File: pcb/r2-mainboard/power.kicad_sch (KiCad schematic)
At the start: 0 parts

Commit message: R2: capture power.kicad_sch -- the gated rail tree from +VSYS
WP2. Five converters, every one of them switchable, which is the whole
reason R2 exists: R1 wires four bucks' ~SHDN to +5V and 82% of idle
power sits on rails no firmware can reach.

  +3V3_AON   TPS7A0233   LDO, always on, 25 nA
  +5V_DCDC   TPS61022    boost, behind a TPS22965 load switch
  +3V3_DCDC  TPS63802    buck-boost
  +1V2_DCDC  TPS62A02    buck
  +1V35_DCDC TPS62A02    buck

Two findings changed the plan and are recorded in NOTES-R2-plan.md:

- A 1S cell cannot buck to 3.3 V. +VSYS runs 4.4 V down to 3.0 V, so a
  step-down converter drops out halfway down the discharge curve. +3V3
  is a buck-boost, and the two 3.3 V rails the plan called for become
  one, since each would cost a whole converter.
- A boost has no load disconnect. Disabling TPS61022 alone would leave
  ~3.4 V on the SoM's VIN pin, which is a partial-power state rather
  than off, so the disconnect goes on the boost's input instead.

Every EN carries a pull-down; the rails come up only when firmware asks.
PG pull-ups are 470k, not 10k, because a power-good pin is low whenever
its rail is off -- at 10k that is 3.3 mW of the 10 mW standby budget.
Converter overhead in standby works out to ~24 uA.

Verified with kicad-cli erc plus a node-by-node read of the exported
netlist. 25 violations, one of them real: battery.kicad_sch's +3V3_AON
PWR_FLAG is now redundant against U10's power_out pin. Left in place --
that sheet is out for review and editing it under an open Eeschema
session would discard unsaved work. docs/power.md §9 has the one-symbol
fix.

Nothing here has been built or measured.

Co-Authored-By: Claude Opus 5 <noreply@anthropic.com>
Claude-Session: https://claude.ai/code/session_01LsKada4AAxqV6Vzap4hwJf
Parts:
- added C20, C21: 1uF/16V, Capacitor_SMD:C_0402_1005Metric, symbol Device:C
- added C22, C25, C26, C27, C30: 22uF/10V, Capacitor_SMD:C_0805_2012Metric, symbol Device:C
- added C23: 470pF/50V, Capacitor_SMD:C_0402_1005Metric, symbol Device:C
- added C24: 100nF/16V, Capacitor_SMD:C_0402_1005Metric, symbol Device:C
- added C28: 100pF/50V, Capacitor_SMD:C_0402_1005Metric, symbol Device:C
- added C29: 10uF/10V, Capacitor_SMD:C_0805_2012Metric, symbol Device:C
- added C31, C33: 4.7uF/10V, Capacitor_SMD:C_0805_2012Metric, symbol Device:C
- added C32, C34: 22uF/6.3V, Capacitor_SMD:C_0805_2012Metric, symbol Device:C
- added L10, L12, L13: 1uH/6A, Inductor_SMD:L_1210_3225Metric, symbol Device:L
- added L11: 0.47uH/6A, Inductor_SMD:L_1008_2520Metric, symbol Device:L
- added R20, R26, R31, R35: 100k, Resistor_SMD:R_0402_1005Metric, symbol Device:R
- added R21: 732k/1%, Resistor_SMD:R_0402_1005Metric, symbol Device:R
- added R22, R29, R30, R34: 100k/1%, Resistor_SMD:R_0402_1005Metric, symbol Device:R
- added R23, R27: 0R, Resistor_SMD:R_0402_1005Metric, symbol Device:R
- added R24: 511k/1%, Resistor_SMD:R_0402_1005Metric, symbol Device:R
- added R25: 91k/1%, Resistor_SMD:R_0402_1005Metric, symbol Device:R
- added R28, R32, R36: 470k, Resistor_SMD:R_0402_1005Metric, symbol Device:R
- added R33: 124k/1%, Resistor_SMD:R_0402_1005Metric, symbol Device:R
- added U10: TPS7A0233DBVR, Package_TO_SOT_SMD:SOT-23-5, symbol r2:TPS7A0233DBV
- added U11: TPS22965DSGR, Package_SON:Texas_DSG0008A_WSON-8-1EP_2x2mm_P0.5mm_EP0.9x1.6mm, symbol r2:TPS22965DSG
- added U12: TPS61022RWUR, Package_DFN_QFN:Texas_RWU0007A_VQFN-7_2x2mm_P0.5mm, symbol Converter_DCDC:TPS61022
- added U13: TPS63802DLAR, r2:Texas_DLA0010A_VSON-HR-10_2x3mm_P0.5mm, symbol r2:TPS63802DLA
- added U14, U15: TPS62A02DRLR, Package_TO_SOT_SMD:SOT-563, symbol r2:TPS62A02DRL
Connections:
- new net: R33.2, R34.1, U15.5 (FB)
- new net: R27.1, U13.2 (MODE)
- new net: R24.2, R25.1, U13.4 (FB)
- new net: L11.2, U13.7 (L2)
- new net: L11.1, U13.9 (L1)
- new net: R29.2, R30.1, U14.5 (FB)
- new net: L13.1, U15.2 (SW)
- new net: L10.2, U12.2 (SW)
- new net: C28.2, R21.2, R22.1, U12.4 (FB)
- new net: L12.1, U14.2 (SW)
- new net: C23.1, U11.6 (CT)
- new net: R23.1, U12.6 (MODE)
- new net +1V2_DCDC: C32.1, L12.2, R29.1
- new net +1V35_DCDC: C34.1, L13.2, R33.1
- new net +3V3_AON: C21.1, R28.1, R32.1, R36.1, U10.5 (OUT)
- new net +3V3_DCDC: C30.1, R24.1, U13.6 (VOUT)
- new net +5V_DCDC: C26.1, C27.1, C28.1, R21.1, U12.3 (VOUT)
- new net +VSYS: C20.1, C22.1, C24.1, C29.1, C31.1, C33.1, U10.1 (IN), U10.3 (EN), U11.1 (VIN), U11.2 (VIN), U11.4 (VBIAS), U13.10 (VIN), U14.3 (VIN), U15.3 (VIN)
- new net GND: C20.2, C21.2, C22.2, C23.2, C24.2, C25.2, C26.2, C27.2, C29.2, C30.2, C31.2, C32.2, C33.2, C34.2, R20.2, R22.2, R23.2, R25.2, R26.2, R27.2, R30.2, R31.2, R34.2, R35.2, U10.2 (GND), U11.5 (GND), U11.9 (EP), U12.1 (GND), U13.3 (AGND), U13.8 (GND), U14.1 (GND), U15.1 (GND)
- new net MCU_EN_3V3: R26.1, U13.1 (EN)
- new net MCU_EN_5V: R20.1, U11.3 (ON)
- new net MCU_EN_DDR: R35.1, U15.4 (EN)
- new net MCU_EN_FPGA_CORE: R31.1, U14.4 (EN)
- new net PG_1V2: R32.2, U14.6 (PG)
- new net PG_1V35: R36.2, U15.6 (PG)
- new net PG_3V3: R28.2, U13.5 (PG)
- new net VSYS_SW: C25.1, L10.1, U11.7 (VOUT), U11.8 (VOUT), U12.5 (EN), U12.7 (VIN)
- no-connect marks 0 -> 1
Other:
- note added: "+1V2_DCDC — Spartan-6 VCCINT"
- note added: "+1V35_DCDC — DDR3L and the FPGA's DDR bank VCCO"
- note added: "+3V3_AON — always-on housekeeping rail"
- note added: "+3V3_DCDC — FPGA I/O, config NOR, microSD"
- note added: "+5V_DCDC — SoM VIN and the EPD HV chain"
- note added: "Buck-boost, not buck: a 1S cell cannot step down to 3.3 V."
- note added: "Dropout is 270 mV max at 200 mA, so the rail follows +VSYS down"
- note added: "ERC power flags"
- note added: "Every EN on this sheet is pulled down, so each rail is off until firmware asks for it."
- note added: "Only the two buck rails need one: their output is the far side"
- note added: "STM32G0, I2C pull-ups, buttons. 25 nA quiescent."
- note added: "That is the whole difference from R1, where four bucks had ~SHDN wired to +5V."
- note added: "True shutdown with load disconnect, so the rail is genuinely"
- note added: "U11 is the real disconnect; U12's EN follows its own switched input,"
- note added: "at low battery. Everything on it works below 3.3 V."
- note added: "of an inductor, so no pin declares itself a driver."
- note added: "off in standby."
- note added: "so one GPIO owns the pair and 'off' is unambiguous."
- note added: "to mcu.kicad_sch"

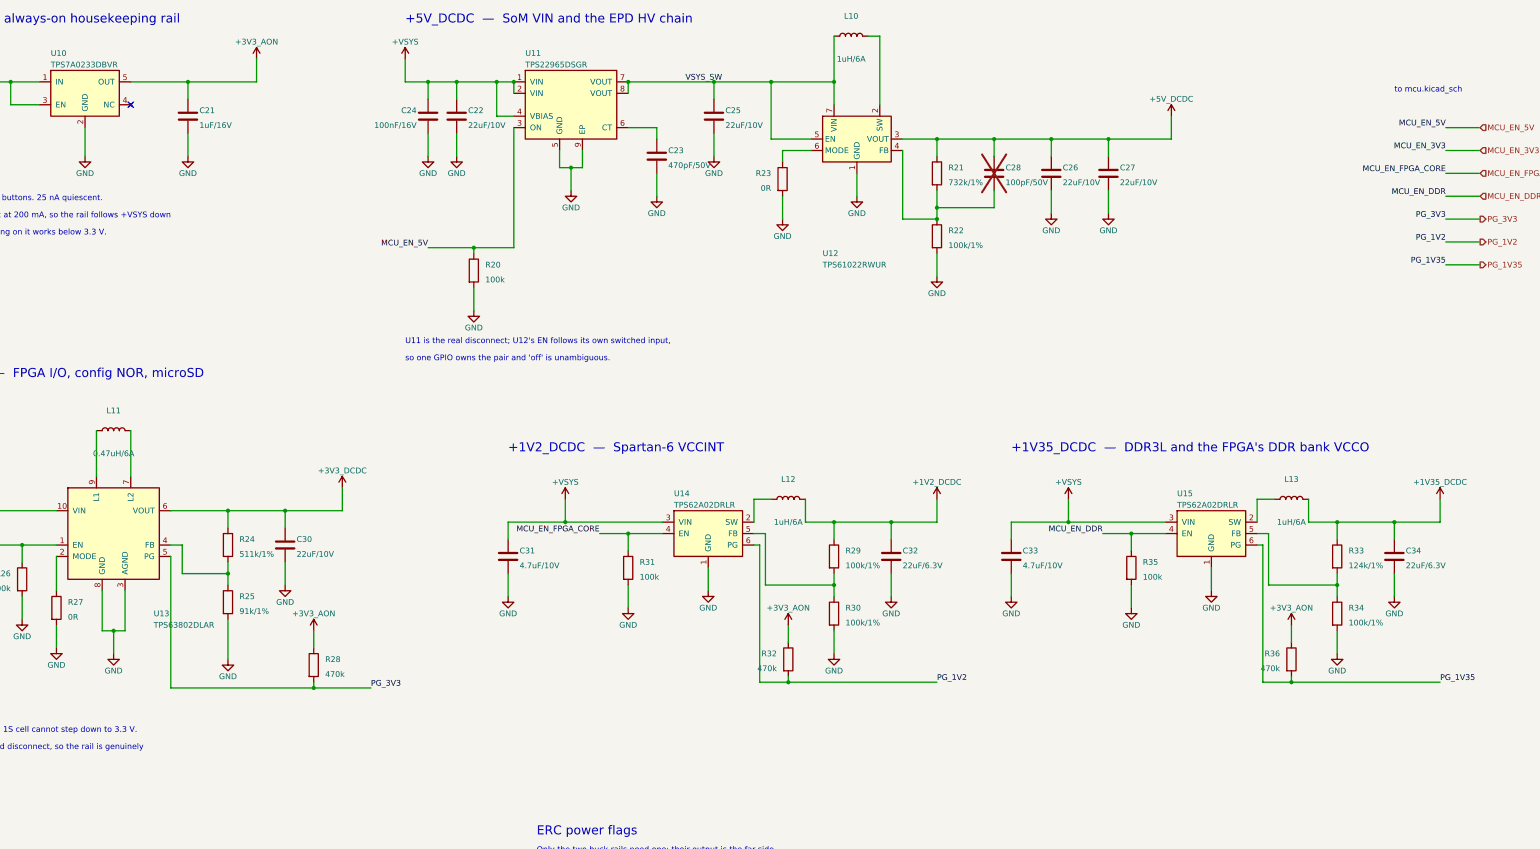
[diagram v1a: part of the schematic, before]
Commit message: R2: power sheet review pass 1 -- the TPS22965 load switch is deleted
power.kicad_sch was reviewed against manual-analysis/Analysis_power.md and
patched in place by tools/patch_power_review1.py. Once Eeschema has saved a
sheet it is the source of truth, so gen_power.py was not re-run.

The substantive finding: the TPS61022 boost already has true input/output
disconnect in shutdown -- datasheet Features (p.1), §7.3.2, and IVOUT_LKG in
§6.5, which is measured with VOUT forced to 5.5 V while VIN sits at 0 V.
docs/power.md §2.2 had misread §7.3.5, which describes pass-through while the
part is *enabled*. U11 (TPS22965) and its C23/C24 are therefore deleted, and
MCU_EN_5V drives U12.EN directly with R20 as the 100 k pull-down. That also
removes ~85 mW of RON loss at 2.3 A and ~30-50 uA of VBIAS quiescent.

Two value errors found while in there: all four inductors claimed 6 A where the
fitted DFE322512F-1R0M is Isat 4.8 A / Irms 3.8 A, and C32/C34 were 6.3 V where
tps62a01.pdf Table 8-3 specifies 10 V.

docs/power.md gains §10 -- all 13 review points answered from the datasheets
with the page or table cited, each closed as either changed or correct-as-drawn
-- and §11, the layout guidelines that §9 owed. §1-§9 and §13 are brought in
line with the patched sheet.

NOTES-R2-plan.md marks WP2 reviewed, withdraws the standing +5V_SOM load-switch
requirement, and closes standing asks 1 and 2 (the +3V3_AON PWR_FLAG must now
stay: after the +3V3_AON_DCDC rename it is the net's only ERC driver).

Verified: kicad-cli sch erc --format json reports 0 violations on /power/; the
netlist was node-diffed against the pre-patch sheet and shows only the intended
changes with no new unconnected-* nets; page 3 was rendered and inspected.

Also included: the owner's own review edits to battery.kicad_sch, and the review
notes moved from Analyse_battery.md to manual-analysis/.

Co-Authored-By: Claude Opus 5 <noreply@anthropic.com>
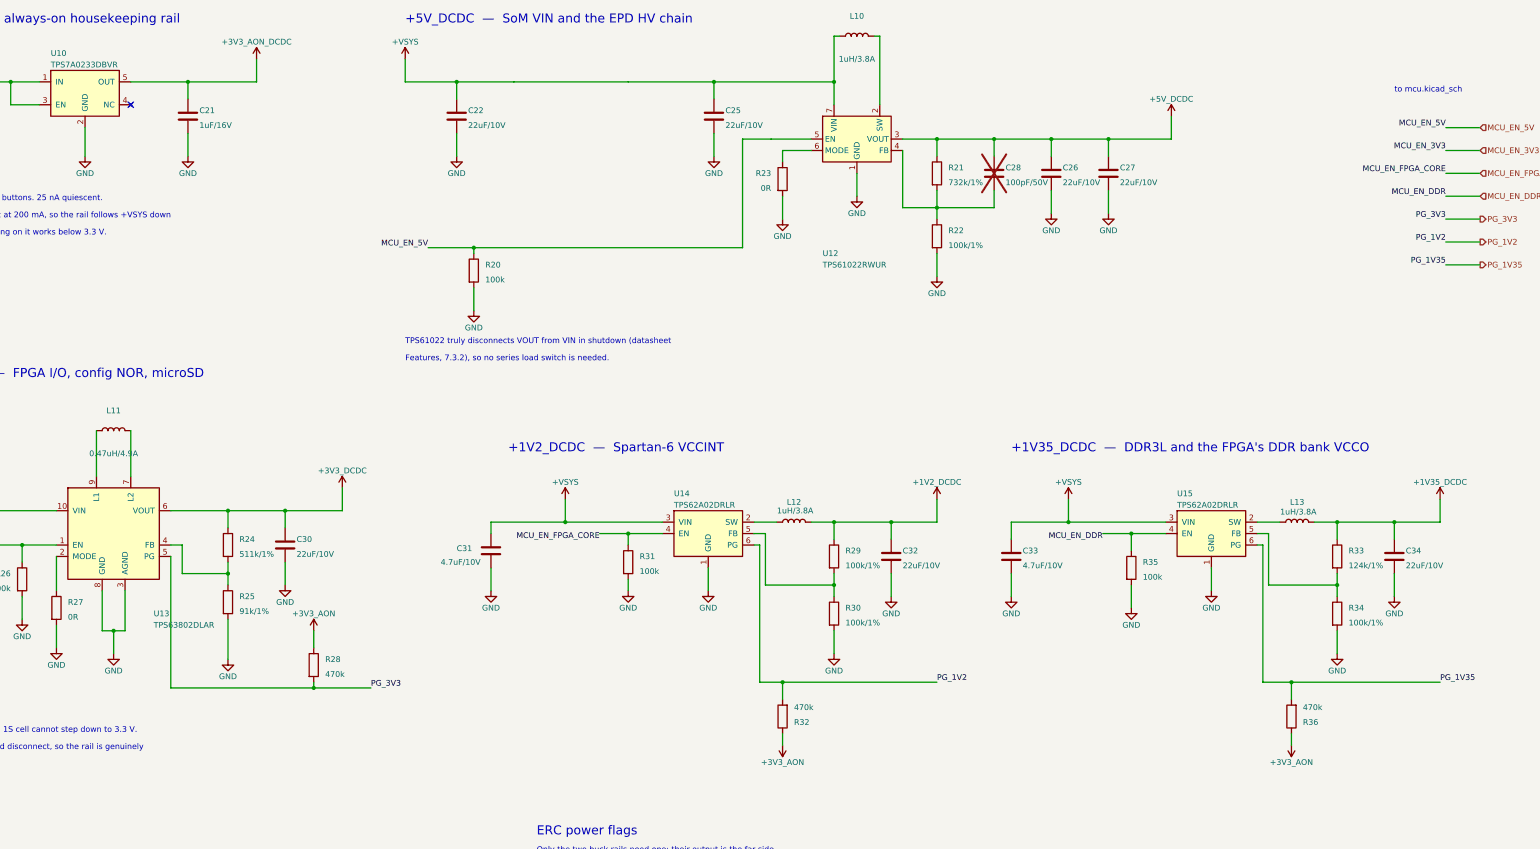
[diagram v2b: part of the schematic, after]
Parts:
- removed C23: 470pF/50V, Capacitor_SMD:C_0402_1005Metric, symbol Device:C
- removed C24: 100nF/16V, Capacitor_SMD:C_0402_1005Metric, symbol Device:C
- removed U11: TPS22965DSGR, Package_SON:Texas_DSG0008A_WSON-8-1EP_2x2mm_P0.5mm_EP0.9x1.6mm, symbol r2:TPS22965DSG
- C32, C34: value 22uF/6.3V -> 22uF/10V
- L10, L12, L13: value 1uH/6A -> 1uH/3.8A
- L11: value 0.47uH/6A -> 0.47uH/4.9A
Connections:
- net +3V3_AON: no longer C21.1, U10.5 (OUT)
- net +VSYS: now also C25.1, L10.1, U12.7 (VIN)
- net MCU_EN_5V: now also U12.5 (EN)
- removed net VSYS_SW: C25.1, L10.1, U12.5 (EN), U12.7 (VIN)
- new net +3V3_AON_DCDC: C21.1, U10.5 (OUT)
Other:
- note added: "Features, 7.3.2), so no series load switch is needed."
- note added: "TPS61022 truly disconnects VOUT from VIN in shutdown (datasheet"
- note removed: "U11 is the real disconnect; U12's EN follows its own switched input,"
- note removed: "so one GPIO owns the pair and 'off' is unambiguous."
- moved on the sheet: C31, L10, L12, L13, R31, R32, R36

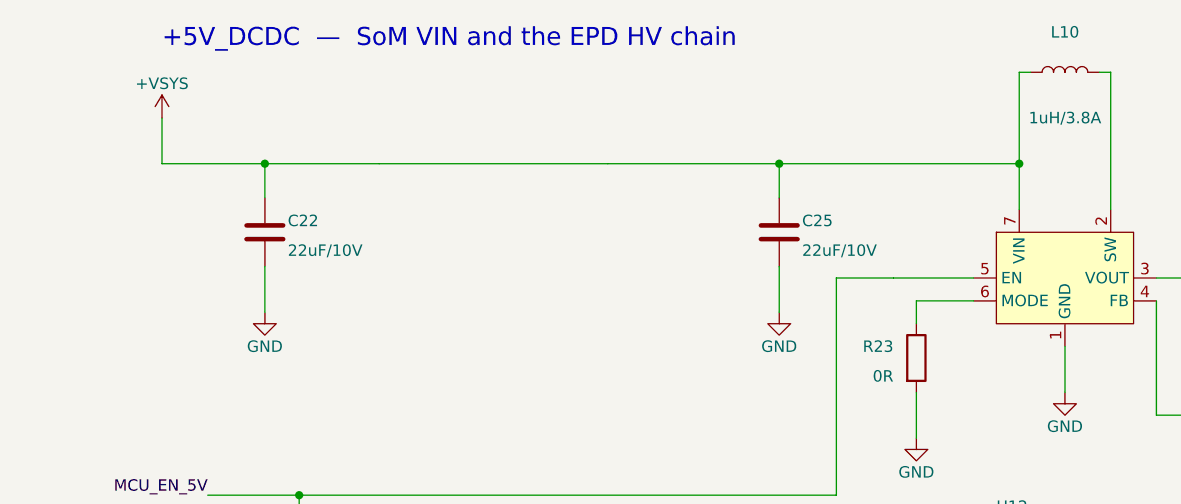
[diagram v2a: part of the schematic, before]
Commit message: R2: mcu sheet review pass 1, plus an R1 comparison
mcu.kicad_sch was reviewed against manual-analysis/Analysis_mcu.md and patched in
place by tools/patch_mcu_review1.py; gen_mcu.py was not re-run.

C42 is deleted. stm32g0b1.pdf Figure 15 (p.65) is the whole of ST's decoupling
scheme and it shows no capacitor on VBAT. With no coin cell fitted, pin 6 (VBAT)
is strapped to the same +3V3_AON net as pin 8 (VDD/VDDA) two pitches away, and
that net already carries C40 4.7 uF + C41 100 nF -- the figure's specified pair.
C42 was a third capacitor on an already-decoupled net.

SW21/SW22, the page buttons, move from TS-1187A-B-A-B to Panasonic EVQPLHA15:
same 1.6 N force and 1.5 mm travel, so the feel is unchanged, but 500 k cycles
instead of 100 k. At a plausible ~200 page turns a day the old part is rated for
about 1.4 years, and these are the most-actuated components on the board. SW20
stays a TS-1187A -- it is the power button, pressed rarely, and JLC Basic.

FB20 stays, but the doc now says plainly that no datasheet asks for it: Figure 15
feeds VREF+ with 100 nF + 1 uF and no series element. It is inherited from R1's
FB3, which was justified because the H750 brings VDDA out as its own pin; the G0
merges VDDA into VDD, so VREF+ is the only node left to filter. What makes it
safe is DCR rather than impedance -- Table 21 caps VREF+ at min(VDD + 0.4, 4.0) V
and BLM15AG121SN1D is 190 mOhm, so 0.19 mV at 1 mA. A resistor there would be a
hazard, and that constraint is now recorded on the part itself.

The 8 MHz the review found is the HSE, not Y20: Table 42 lists fOSC_IN as 4/8/48
MHz min/typ/max and Figure 20 is captioned "Typical application with an 8 MHz
crystal". Y20 is the LSE -- Table 43, on PC14/PC15. No HSE is fitted, which is
what frees PF0/PF1 for MCU_EN_5V/MCU_EN_3V3.

Datasheet 3.5 (p.16) lists the boot loader's interfaces and two are already on
this sheet: USART on PA9/PA10 (= MCU_TXD/MCU_RXD, with the SoM at the far end)
and USB on PA11/PA12 (two of the eleven spa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
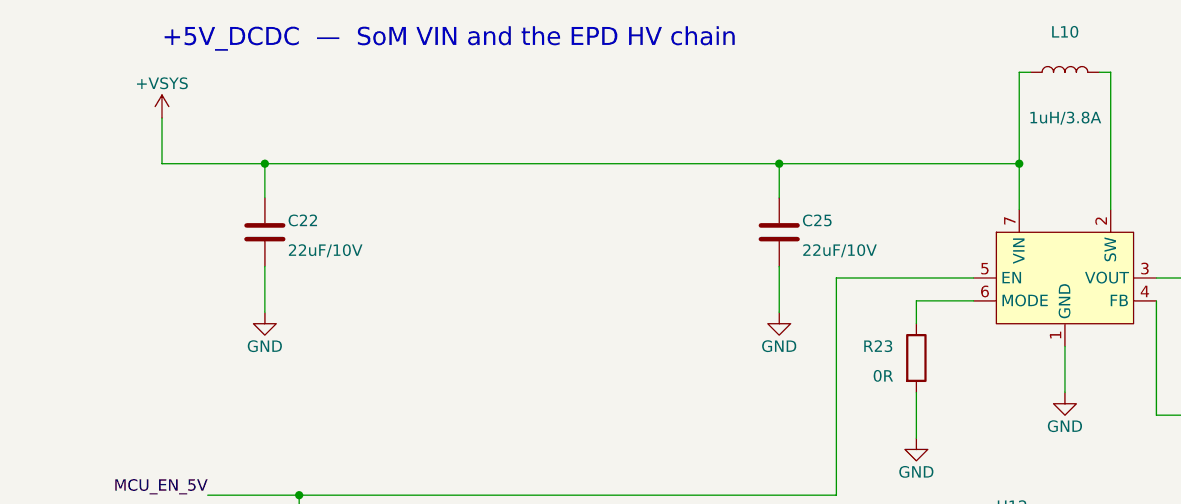
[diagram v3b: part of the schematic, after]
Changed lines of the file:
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@@
 	(wire
 		(pts
-			(xy 140.97 58.42) (xy 165.1 58.42)
+			(xy 140.97 58.42) (xy 236.22 58.42)
 		)
 		(stroke
@@
 	(wire
 		(pts
+			(xy 146.05 95.25) (xy 215.9 95.25)
+		)
+		(stroke
+			(width 0)
+			(type default)
+		)
+	)
+	(wire
+		(pts
 			(xy 370.84 156.21) (xy 370.84 151.13)
 		)
@@
 	(wire
 		(pts
-			(xy 222.25 71.12) (xy 231.14 71.12)
-		)
-		(stroke
-			(width 0)
-			(type default)
-		)
-	)
-	(wire
-		(pts
 			(xy 236.22 180.34) (xy 236.22 185.42)
 		)
@@
 	(wire
 		(pts
-			(xy 245.11 48.26) (xy 246.38 48.26)
+			(xy 215.9 95.25) (xy 215.9 71.12)
 		)
 		(stroke
@@
 	(wire
 		(pts
-			(xy 231.14 73.66) (xy 224.79 73.66)
+			(xy 245.11 48.26) (xy 246.38 48.26)
 		)
 		(stroke
@@
 	(wire
 		(pts
-			(xy 297.18 71.12) (xy 297.18 74.93)
+			(xy 231.14 73.66) (xy 224.79 73.66)
 		)
 		(stroke
@@
 	(wire
 		(pts
-			(xy 190.5 58.42) (xy 236.22 58.42)
+			(xy 297.18 71.12) (xy 297.18 74.93)
 		)
 		(stroke
@@
 	(wire
 		(pts
+			(xy 215.9 71.12) (xy 231.14 71.12)
+		)
+		(stroke
+			(width 0)
+			(type default)
+		)
+	)
+	(wire
+		(pts
 			(xy 88.9 153.67) (xy 127 153.67)
 		)
@@
 		)
 	)
-	(wire
-		(pts
-			(xy 165.1 58.42) (xy 190.5 58.42)
-		)
-		(stroke
-			(width 0)
-			(type default)
-		)
-	)
-	(wire
-		(pts
-			(xy 146.05 95.25) (xy 215.9 95.25)
-		)
-		(stroke
-			(width 0)
-			(type default)
-		)
-	)
-	(wire
-		(pts
-			(xy 215.9 95.25) (xy 215.9 71.12)
-		)
-		(stroke
-			(width 0)
-			(type default)
-		)
-	)
-	(wire
-		(pts
-			(xy 215.9 71.12) (xy 222.25 71.12)
-		)
-		(stroke
-			(width 0)
-			(type default)
-		)
-	)
